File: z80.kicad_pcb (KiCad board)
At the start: 2 copper layers, 104.1 x 121.9 mm, 53 parts, among them P1 CONN_02X20, SW1 RESET, SW2 STEP, U1 Z80CPU, U2 74HC04, U3 74LS138, U4 LM555N, U5 74HC74, U6 LM555N, Y1 7.3728MHz

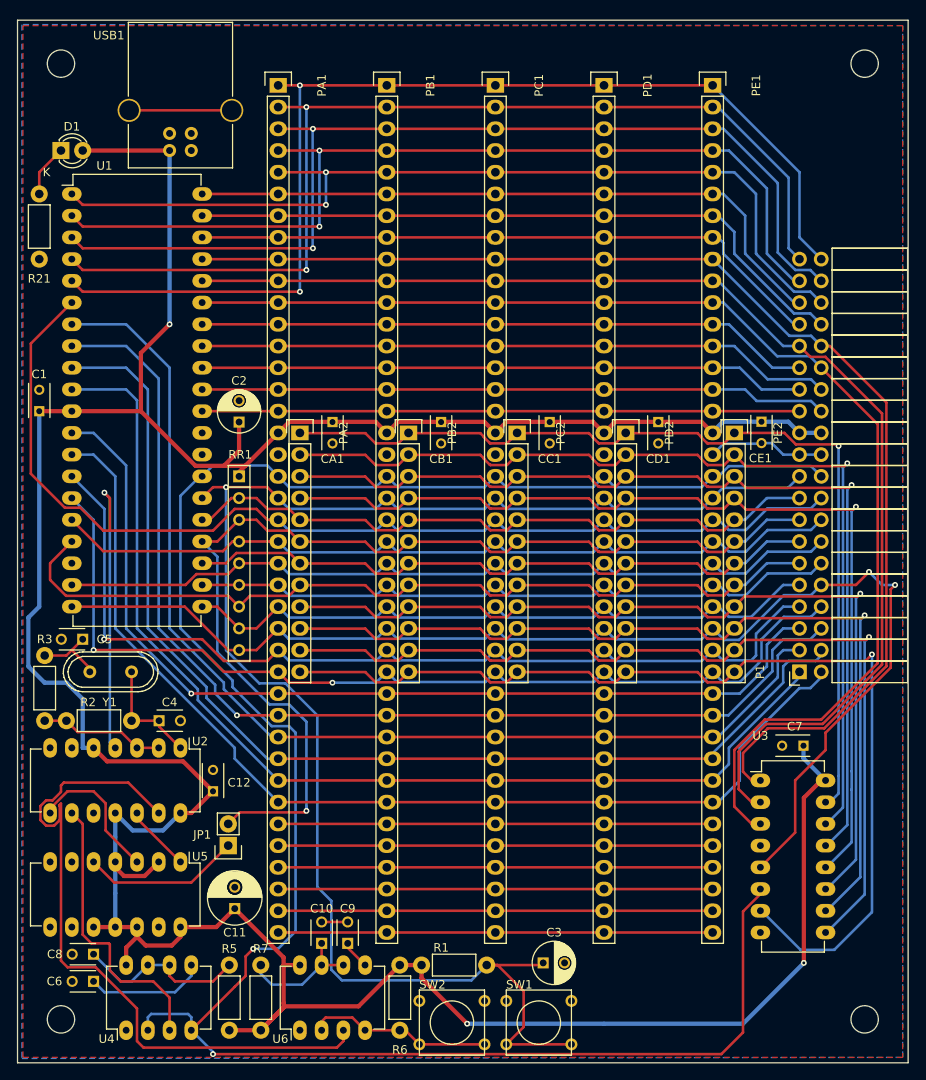
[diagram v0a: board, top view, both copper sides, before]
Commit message: Another new board layout. Few tidy ups.
Removed the single step circuit, not worth the board space and headache.
Added legend for the IO slot for easy reference. Still toying where to
put the power LED, annoying me with that resistor. Think I'm happy with
it now. Spaced things out a little to make it easy for manufacture, made
sure no traces are near board edges as much as possible.
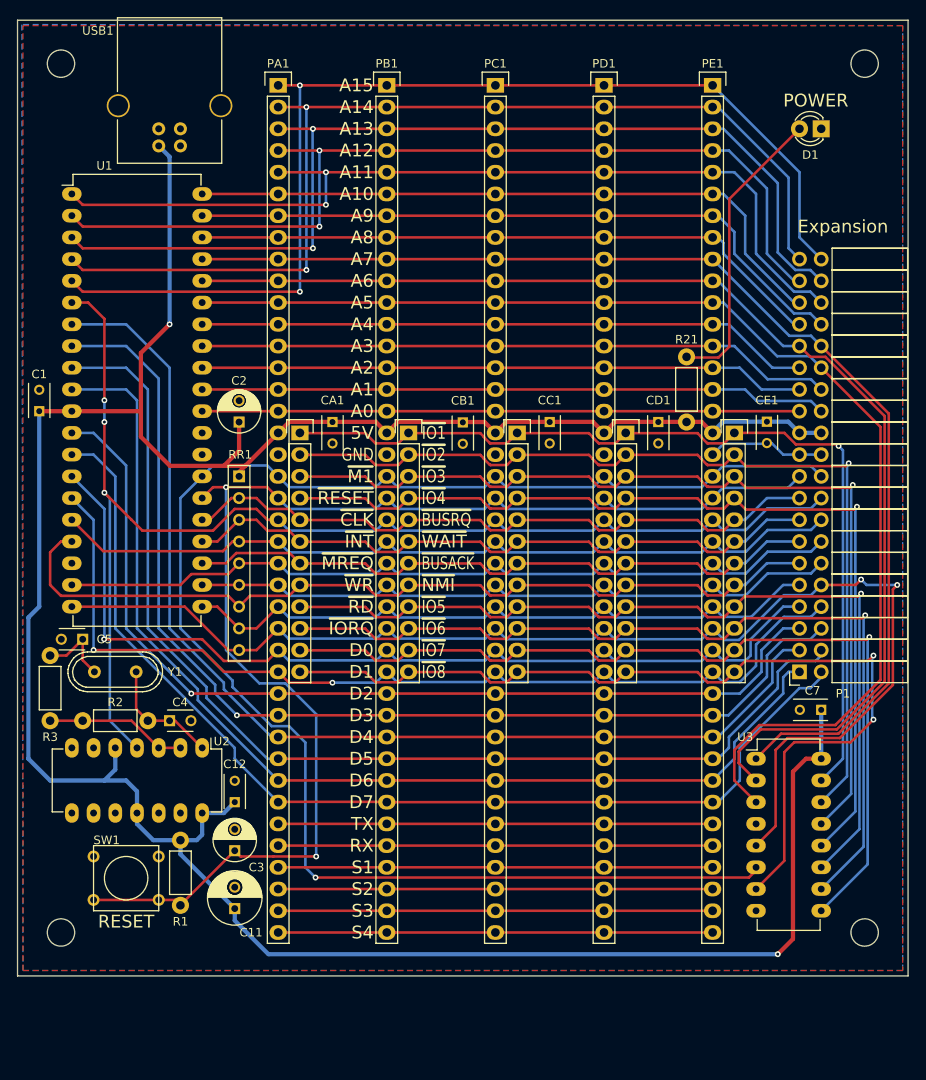
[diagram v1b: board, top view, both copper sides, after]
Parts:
- removed C10, C6, C8, C9: 10n, Capacitors_ThroughHole:C_Disc_D3_P2.5
- removed G***: LOGO, ncr2016_logo:nrc2016_logo_1200
- removed JP1: JUMPER, Pin_Headers:Pin_Header_Straight_1x02
- removed R5, R7: 1K, Resistors_ThroughHole:Resistor_Horizontal_RM7mm
- removed R6: 10K, Resistors_ThroughHole:Resistor_Horizontal_RM7mm
- removed SW2: STEP, Buttons_Switches_ThroughHole:SW_PUSH_SMALL
- removed U4, U6: LM555N, Housings_DIP:DIP-8_W7.62mm_LongPads
- removed U5: 74HC74, Housings_DIP:DIP-14_W7.62mm_LongPads
- moved D1 88.9 mm to (134.6, 43.2), turned to 180 degrees
- moved R21 80.3 mm to (118.9, 77.5), turned to 90 degrees
- moved SW1 51.1 mm to (53.3, 130.8)
- moved C3 38.4 mm to (66.0, 127.6), turned to 90 degrees
- moved R1 31.8 mm to (59.7, 126.4), turned to 270 degrees
- moved MH3 10.2 mm to (45.7, 137.2)
- moved MH4 10.2 mm to (139.7, 137.2)
- moved C7 4.68 mm to (134.6, 111.1)
- moved C12 2.84 mm to (66.0, 121.9)
- moved U3 2.59 mm to (127.0, 116.8)
- moved CB1 2.54 mm to (92.7, 77.5)
- moved U2 2.54 mm to (62.2, 115.6)
- moved R2 1.91 mm to (48.3, 112.4)
- moved USB1 1.38 mm to (57.1, 45.2)
- moved C4 1.23 mm to (58.4, 112.4)
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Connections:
- D1 pad 1: Net-(D1-Pad1) -> GND
- D1 pad 2: VCC -> Net-(D1-Pad2)
- R21 pad 1: Net-(D1-Pad1) -> VCC
- R21 pad 2: GND -> Net-(D1-Pad2)
- U2 pad 12: Net-(U2-Pad12) -> (no net)
- U2 pad 13: Net-(U2-Pad13) -> (no net)
- U2 pad 8: Net-(U2-Pad8) -> (no net)
- U2 pad 9: Net-(U2-Pad9) -> (no net)
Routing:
- net Net-(U2-Pad13): track 82.8 -> 0.00 mm
- net /~M1: track 251.1 -> 186.6 mm, vias 2 -> 1
- net VCC: track 394.9 -> 331.1 mm, vias 3 -> 2
- net /~WAIT: track 125.2 -> 77.0 mm, vias 1 -> 0
- net Net-(D1-Pad2): track 0.00 -> 34.4 mm
- net Net-(U2-Pad9): track 33.6 -> 0.00 mm
- net /~RESET: track 185.9 -> 154.7 mm, vias 1 -> 2
- net Net-(R6-Pad2): track 21.6 -> 0.00 mm
- net Net-(C8-Pad1): track 20.3 -> 0.00 mm
- net Net-(JP1-Pad1): track 18.5 -> 0.00 mm
- net Net-(U2-Pad8): track 16.8 -> 0.00 mm
- net Net-(C10-Pad1): track 14.7 -> 0.00 mm
- net Net-(C6-Pad1): track 14.0 -> 0.00 mm
- net Net-(USB1-Pad5): track 12.0 -> 0.00 mm
- net /~CLK: track 160.1 -> 149.8 mm, vias 1 -> 3
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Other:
- board size 104.1 x 121.9 mm -> 104.1 x 111.8 mm
- board text added: "5V"
- board text added: "A0"
- board text added: "A1"
- board text added: "A10"
- board text added: "A11"
- board text added: "A12"
- board text added: "A13"
- board text added: "A14"
- board text added: "A15"
- board text added: "A2"
- board text added: "A3"
- board text added: "A4"
- board text added: "A5"
- board text added: "A6"
- board text added: "A7"
- board text added: "A8"
- board text added: "A9"
- board text added: "D0"
- board text added: "D1"
- board text added: "D2"
- board text added: "D3"
- board text added: "D4"
- board text added: "D5"
- board text added: "D6"
- board text added: "D7"
- board text added: "Expansion"
- board text added: "GND"
- board text added: "POWER"
- board text added: "RESET"
- board text added: "RX"
- board text added: "S1"
- board text added: "S2"
- board text added: "S3"
- board text added: "S4"
- board text added: "TX"
- board text added: "~BUSACK"
- board text added: "~BUSRQ"
- board text added: "~CLK"
- board text added: "~INT"
- board text added: "~IO1"
- board text added: "~IO2"
- board text added: "~IO3"
- board text added: "~IO4"
- board text added: "~IO5"
- board text added: "~IO6"
- board text added: "~IO7"
- board text added: "~IO8"
- board text added: "~IORQ"
- board text added: "~M1"
- board text added: "~MREQ"
- board text added: "~NMI"
- board text added: "~RD"
- board text added: "~RESET"
- board text added: "~WAIT"
- board text added: "~WR"

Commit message: Hopefully the final layout
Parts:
- added G***: LOGO, ncr2016_logo:nrc2016_logo_1200, B.Cu at (54.6, 74.9)
- moved R21 34.2 mm to (141.7, 52.1), turned to 180 degrees
- moved D1 4.37 mm to (137.2, 46.7)
- moved CD1 4.09 mm to (118.7, 80.0)
- moved U3 4.07 mm to (129.5, 113.7)
- moved CB1 3.40 mm to (89.5, 78.7)
- moved PB1 2.54 mm to (86.4, 38.1)
- moved PB2 2.54 mm to (83.8, 78.7)
- moved PC1 2.54 mm to (99.1, 38.1)
- moved PC2 2.54 mm to (96.5, 78.7)
- moved PD1 2.54 mm to (111.8, 38.1)
- moved PD2 2.54 mm to (109.2, 78.7)
- moved PA1 2.54 mm to (73.7, 38.1)
- moved PA2 2.54 mm to (71.1, 78.7)
- moved PE1 2.54 mm to (124.5, 38.1)
- moved PE2 2.54 mm to (121.9, 78.7)
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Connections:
- U1 pad 18: (no net) -> /CPU/~HALT
- U1 pad 28: (no net) -> Net-(U1-Pad28)
- U2 pad 10: (no net) -> Net-(U2-Pad10)
- U2 pad 6: (no net) -> Net-(U2-Pad6)
- USB1 pad 2: (no net) -> Net-(USB1-Pad2)
- USB1 pad 3: (no net) -> Net-(USB1-Pad3)
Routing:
- net /~M1: track 186.6 -> 125.3 mm
- net VCC: track 331.1 -> 390.4 mm, vias 2 -> 1
- net Net-(D1-Pad2): track 34.4 -> 5.54 mm
- net /Card Slots/~IOSEL8: track 108.9 -> 83.8 mm, vias 2 -> 0
- net /~IORQ: track 148.4 -> 124.8 mm, vias 2 -> 1
- net GND: track 13.8 -> 31.9 mm, vias 0 -> 1
- net Net-(USB1-Pad5): track 0.00 -> 12.0 mm
- net /~RESET: track 154.7 -> 147.6 mm, vias 2 -> 0
- net /A5: track 142.6 -> 138.5 mm
- net /A6: track 142.1 -> 138.1 mm
- net /D0: track 111.8 -> 107.9 mm
- net /D1: track 114.6 -> 110.8 mm, vias 2 -> 1
- net /A15: track 127.7 -> 131.5 mm, vias 2 -> 0
- net /A11: track 108.0 -> 104.4 mm, vias 2 -> 0
- net /Card Slots/~IOSEL6: track 104.9 -> 101.5 mm
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
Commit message: Can't help myself, damn you OCD!
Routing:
- net VCC: track 390.4 -> 389.7 mm
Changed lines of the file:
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@@
     (thickness 1.6002)
     (drawings 63)
-    (tracks 1093)
+    (tracks 1092)
     (zones 0)
     (modules 41)
@@
   (gr_line (start 40.64 142.24) (end 40.64 30.48) (angle 90) (layer Edge.Cuts) (width 0.1))
   (gr_line (start 40.64 30.48) (end 144.78 30.48) (angle 90) (layer Edge.Cuts) (width 0.1))
+  (segment (start 43.18 76.2) (end 42.672 76.708) (width 0.5) (layer Bottom) (net 1))
+  (segment (start 42.672 76.708) (end 42.672 117.602) (width 0.5) (layer Bottom) (net 1))
+  (segment (start 42.672 117.602) (end 44.45 119.38) (width 0.5) (layer Bottom) (net 1))
+  (segment (start 44.45 119.38) (end 50.8 119.38) (width 0.5) (layer Bottom) (net 1))
   (segment (start 140.97 72.39) (end 140.97 52.832) (width 0.5) (layer Bottom) (net 1))
   (segment (start 140.97 52.832) (end 141.732 52.07) (width 0.5) (layer Bottom) (net 1))
@@
   (segment (start 54.61 120.65) (end 54.61 123.19) (width 0.5) (layer Bottom) (net 1))
   (segment (start 50.8 119.38) (end 53.34 119.38) (width 0.5) (layer Bottom) (net 1))
-  (segment (start 43.18 76.2) (end 43.18 99.06) (width 0.5) (layer Bottom) (net 1))
-  (segment (start 43.18 99.06) (end 41.91 100.33) (width 0.5) (layer Bottom) (net 1))
-  (segment (start 41.91 100.33) (end 41.91 116.84) (width 0.5) (layer Bottom) (net 1))
-  (segment (start 41.91 116.84) (end 44.45 119.38) (width 0.5) (layer Bottom) (net 1))
-  (segment (start 44.45 119.38) (end 50.8 119.38) (width 0.5) (layer Bottom) (net 1))
   (segment (start 50.8 119.38) (end 52.07 118.11) (width 0.5) (layer Bottom) (net 1))
   (segment (start 52.07 118.11) (end 52.07 116.713) (width 0.5) (layer Bottom) (net 1))

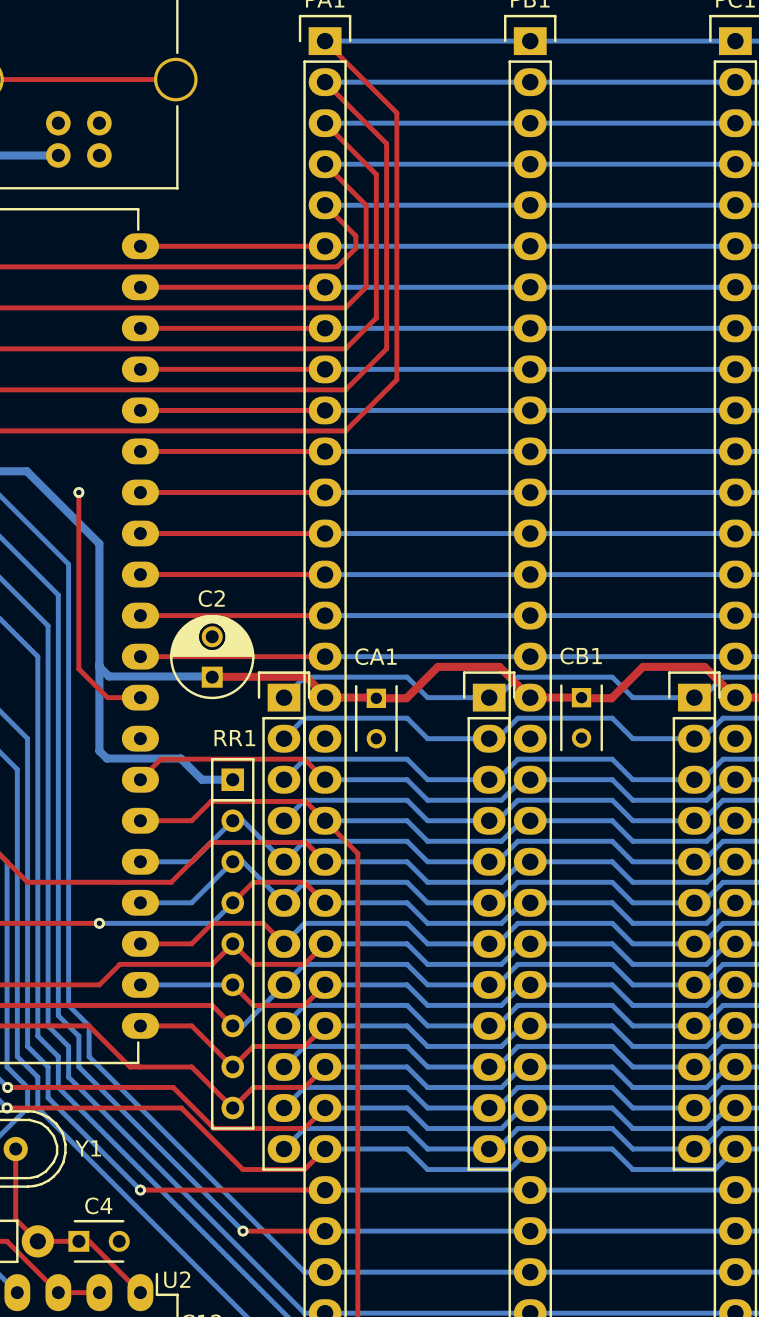
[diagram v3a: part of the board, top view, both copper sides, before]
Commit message: * added USB data signals to first slot * added logo to the top of the board. * added logo PNG files.
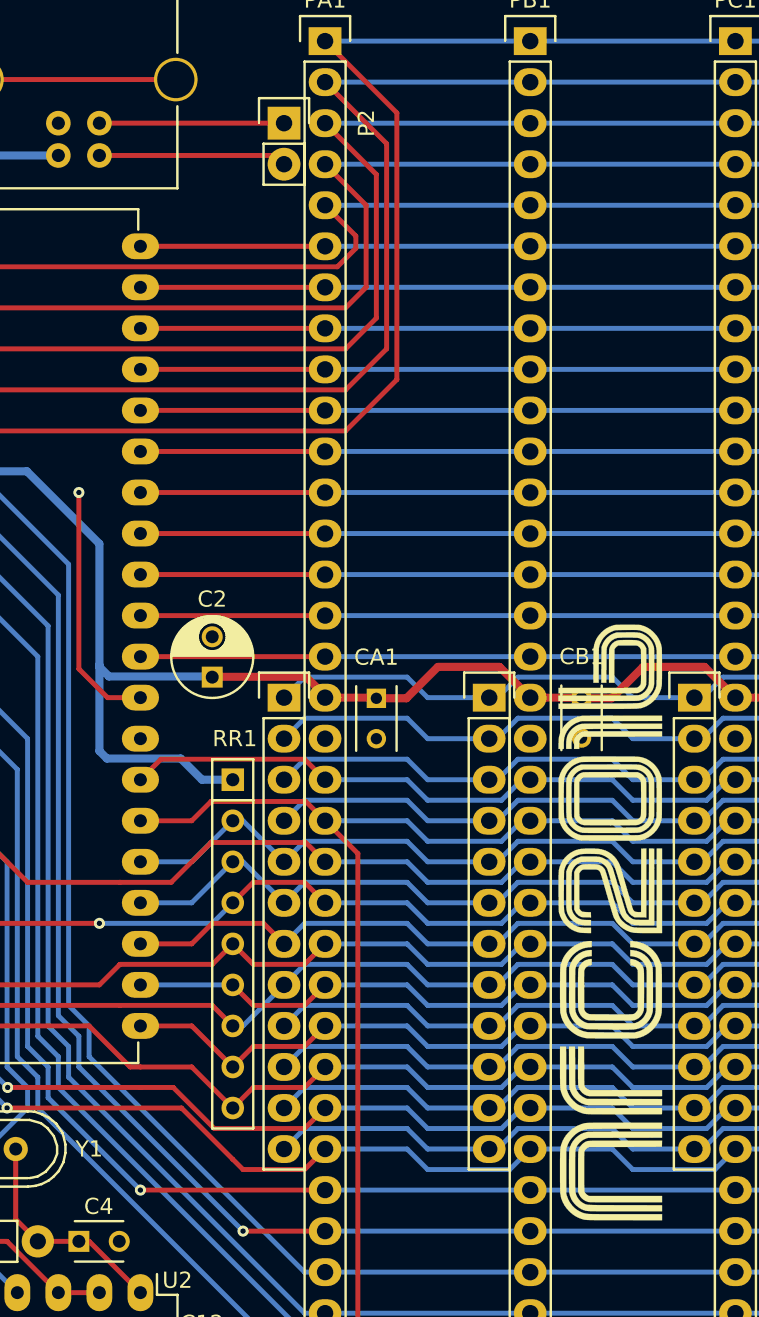
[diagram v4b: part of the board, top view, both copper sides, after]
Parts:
- added G***: LOGO, ncr2016_logo:nrc2016_top_logo_1600, F.Cu at (91.4, 92.7)
- added P2: CONN_01X02, Socket_Strips:Socket_Strip_Straight_1x02, F.Cu at (71.1, 43.2)
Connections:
- net /A0 renamed /CPU/A0
- net /A1 renamed /CPU/A1
- net /A10 renamed /CPU/A10
- net /A11 renamed /CPU/A11
- net /A12 renamed /CPU/A12
- net /A13 renamed /CPU/A13
- net /A14 renamed /CPU/A14
- net /A15 renamed /CPU/A15
- net /A2 renamed /CPU/A2
- net /A3 renamed /CPU/A3
- net /A4 renamed /CPU/A4
- net /A5 renamed /CPU/A5
- net /A6 renamed /CPU/A6
- net /A7 renamed /CPU/A7
- net /A8 renamed /CPU/A8
- net /A9 renamed /CPU/A9
- net /Card Slots/RX renamed /Card Slots/PortA/RX
- net /Card Slots/S1 renamed /Card Slots/PortA/SPARE1
- net /Card Slots/S2 renamed /Card Slots/PortA/SPARE2
- net /Card Slots/S3 renamed /Card Slots/PortA/SPARE3
- net /Card Slots/S4 renamed /Card Slots/PortA/SPARE4
- net /Card Slots/TX renamed /Card Slots/PortA/TX
- net /Card Slots/~IOSEL1 renamed /Card Slots/PortA/~IOSEL1
- net /Card Slots/~IOSEL2 renamed /Card Slots/PortA/~IOSEL2
- net /Card Slots/~IOSEL3 renamed /Card Slots/PortA/~IOSEL3
- net /Card Slots/~IOSEL4 renamed /Card Slots/PortA/~IOSEL4
- net /Card Slots/~IOSEL5 renamed /Card Slots/PortA/~IOSEL5
- net /Card Slots/~IOSEL6 renamed /Card Slots/PortA/~IOSEL6
- net /Card Slots/~IOSEL7 renamed /Card Slots/PortA/~IOSEL7
- net /Card Slots/~IOSEL8 renamed /Card Slots/PortA/~IOSEL8
- net /D0 renamed /CPU/D0
- net /D1 renamed /CPU/D1
- net /D2 renamed /CPU/D2
- net /D3 renamed /CPU/D3
- net /D4 renamed /CPU/D4
- net /D5 renamed /CPU/D5
- net /D6 renamed /CPU/D6
- net /D7 renamed /CPU/D7
- net /~BUSACK renamed /CPU/~BUSACK
- net /~BUSRQ renamed /CPU/~BUSRQ
- net /~CLK renamed /CPU/~CLK
- net /~INT renamed /CPU/~INT
- net /~IORQ renamed /CPU/~IORQ
- net /~M1 renamed /CPU/~M1
- net /~MREQ renamed /CPU/~MREQ
- net /~NMI renamed /CPU/~NMI
- net /~RD renamed /CPU/~RD
- net /~RESET renamed /CPU/~RESET
- net /~WAIT renamed /CPU/~WAIT
- net /~WR renamed /CPU/~WR
- U1 pad 18: /CPU/~HALT -> (no net)
- U1 pad 28: Net-(U1-Pad28) -> (no net)
- U2 pad 10: Net-(U2-Pad10) -> (no net)
- U2 pad 6: Net-(U2-Pad6) -> (no net)
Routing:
- net Net-(P2-Pad2): track 0.00 -> 11.7 mm
- net Net-(P2-Pad1): track 0.00 -> 11.4 mm
